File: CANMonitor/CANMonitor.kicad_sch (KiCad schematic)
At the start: 8 parts, among them J1 Screw_Terminal_01x04, J2 Screw_Terminal_01x04, U1 MCP2558FD-xSN

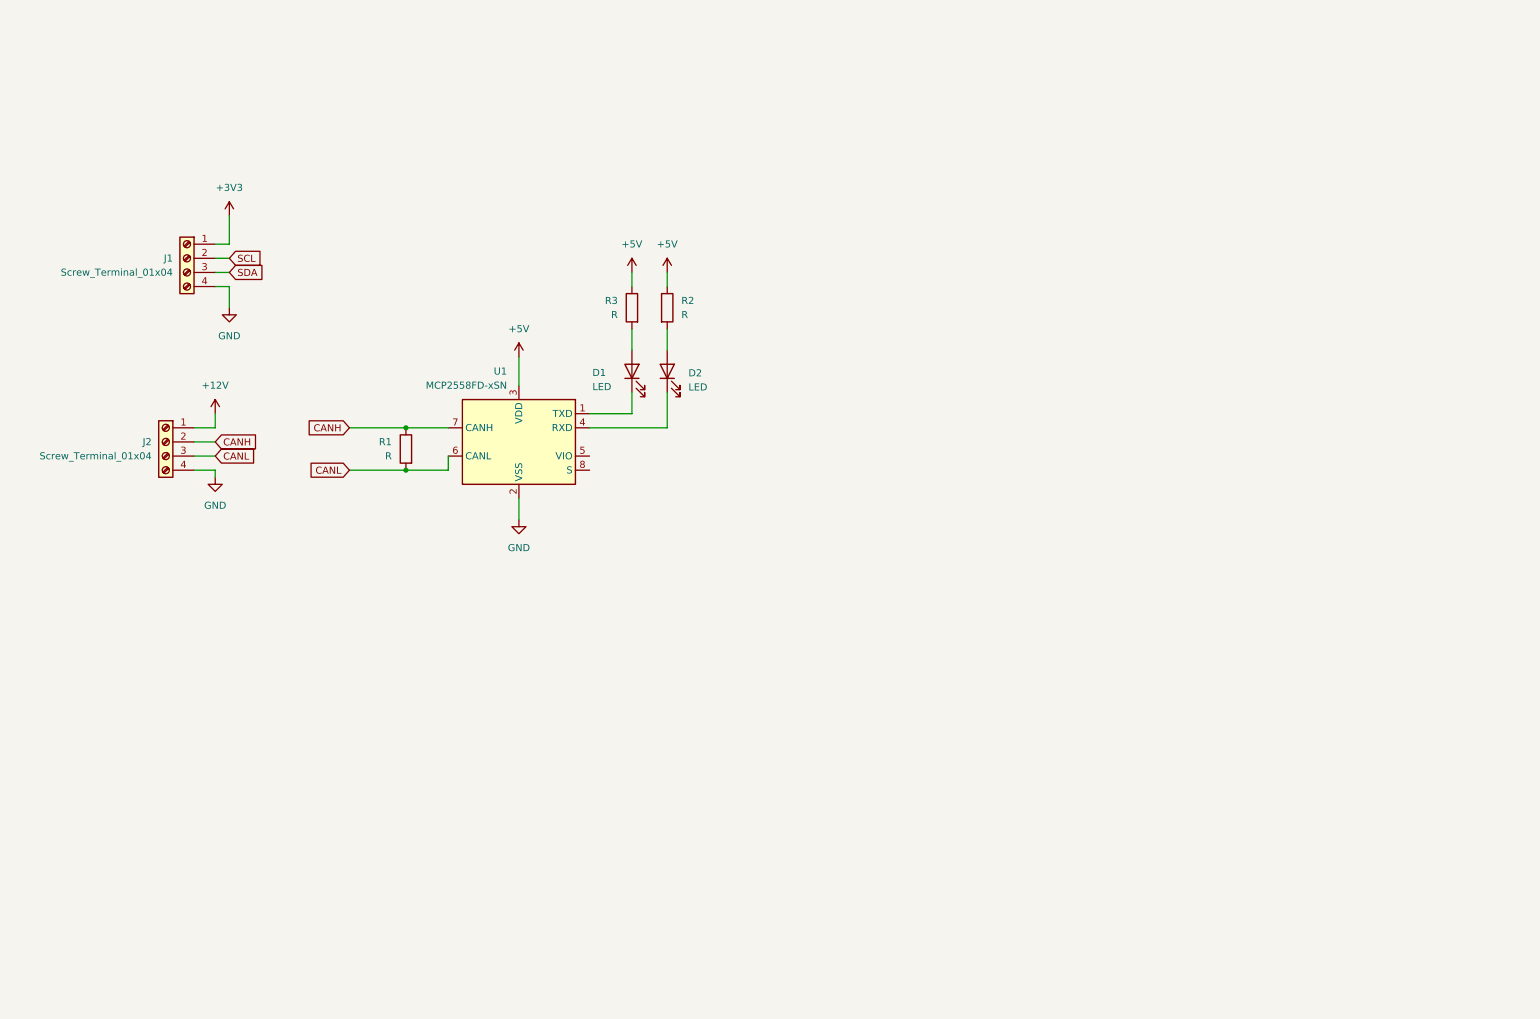
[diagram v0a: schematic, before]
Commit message: Added MCU, netlist, and organized into modules.
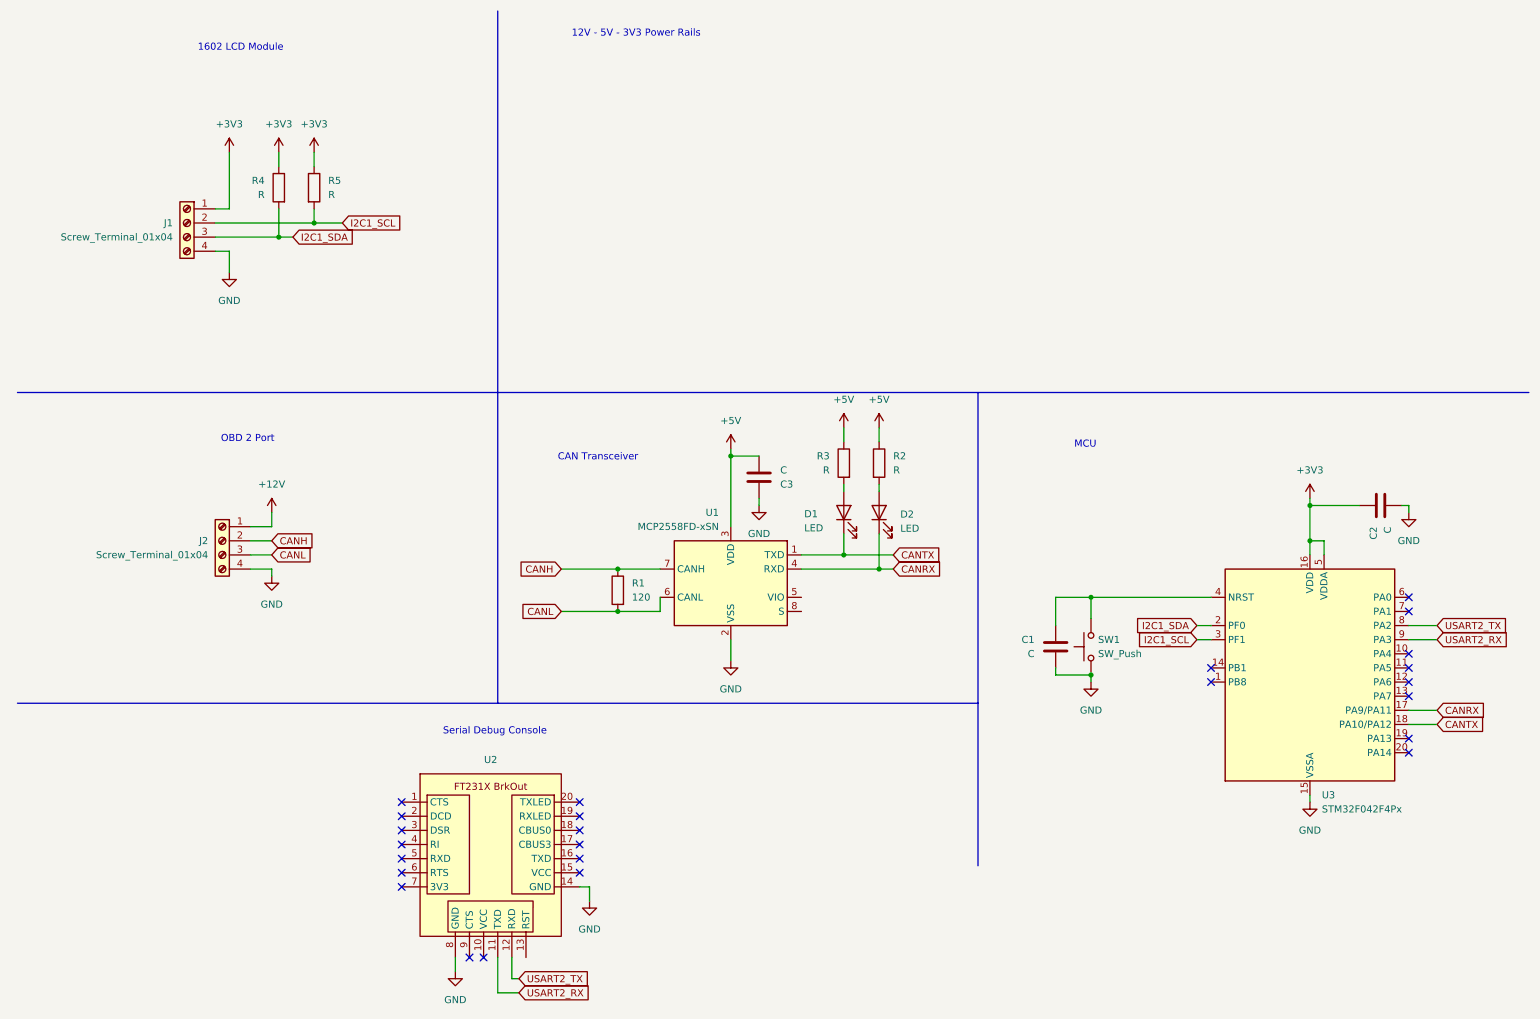
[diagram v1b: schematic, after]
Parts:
- added C1, C2, C3: C, symbol Device:C
- added R4, R5: R, symbol Device:R
- added SW1: SW_Push, symbol Switch:SW_Push
- added U2: (no value), symbol Local_Hats:HEADER_FTDI
- added U3: STM32F042F4Px, Package_SO:TSSOP-20_4.4x6.5mm_P0.65mm, symbol MCU_ST_STM32F0:STM32F042F4Px
- R1: value R -> 120
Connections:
- net +3V3: now also C2.1, R4.1, R5.1, U3.16 (VDD), U3.5 (VDDA)
- net +5V: now also C3.2
- net GND: now also C1.2, C2.2, C3.1, SW1.1, U2.14 (GND), U2.8 (GND), U3.15 (VSSA)
- net CANRX: now reaches D2.1 (K), U1.4 (RXD)
- net CANRX: now also U3.17 (PA9/PA11)
- net CANTX: now reaches D1.1 (K), U1.1 (TXD)
- net CANTX: now also U3.18 (PA10/PA12)
- net SCL renamed I2C1_SCL
- net I2C1_SCL: now also R5.2, U3.3 (PF1)
- net SDA renamed I2C1_SDA
- net I2C1_SDA: now also R4.2, U3.2 (PF0)
- new net: C1.1, SW1.2, U3.4 (NRST)
- new net USART2_RX: U2.11 (TXD), U3.9 (PA3)
- new net USART2_TX: U2.12 (RXD), U3.8 (PA2)
- no-connect marks 0 -> 25
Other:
- note added: "12V - 5V - 3V3 Power Rails"
- note added: "1602 LCD Module"
- note added: "CAN Transceiver"
- note added: "MCU"
- note added: "OBD 2 Port"
- note added: "Serial Debug Console"
- title: (none) -> CANMonitor
- moved on the sheet: D1, D2, J1, J2, R1, R2, R3, U1

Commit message: Created Local Symbols and Added SWD Interface
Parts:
- removed J1, J2: Screw_Terminal_01x04, symbol Connector:Screw_Terminal_01x04
- removed SW1: SW_Push, symbol Switch:SW_Push
- added J3: (no value), symbol Local_Header:Header_Pin_1x4_2.54mm
- added SW1: Switch_PushBtn, symbol Local_Switches:Switch_PushBtn
- added TB1, TB2: (no value), symbol Local_ScrewTerm:Screw_Terminal_01x04
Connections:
- net +12V: now also TB2.1
- net +3V3: now also J3.1, TB1.1
- net CANH: now also TB2.2
- net CANL: now also TB2.3
- net GND: now also J3.5, SW1.2, TB1.4, TB2.4
- net I2C1_SCL: now also TB1.2
- net I2C1_SDA: now also TB1.3
- net NRST: now reaches C1.1, U3.4 (NRST)
- net NRST: now also J3.4, SW1.1
- net SWDIO: now reaches U3.19 (PA13)
- net SWDIO: now also J3.2
- net SWCLK: now reaches U3.20 (PA14)
- net SWCLK: now also J3.3
- no-connect marks 25 -> 24
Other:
- note added: "SWD Header"

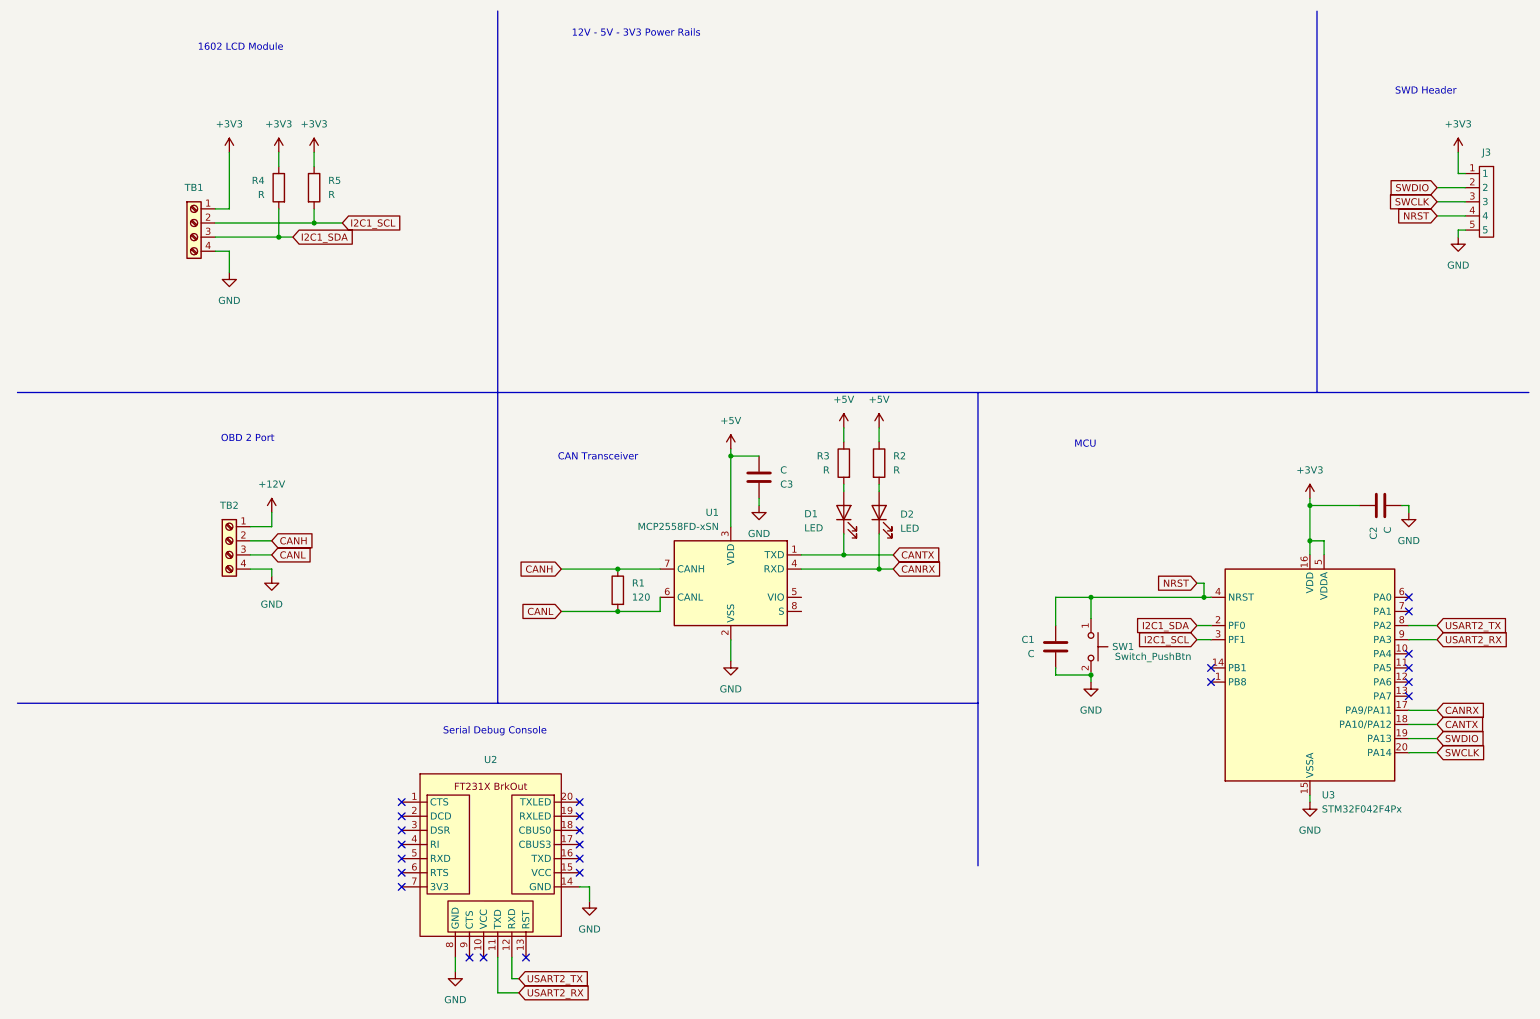
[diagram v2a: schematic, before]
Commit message: Added Custom Symbols and Power LEDs
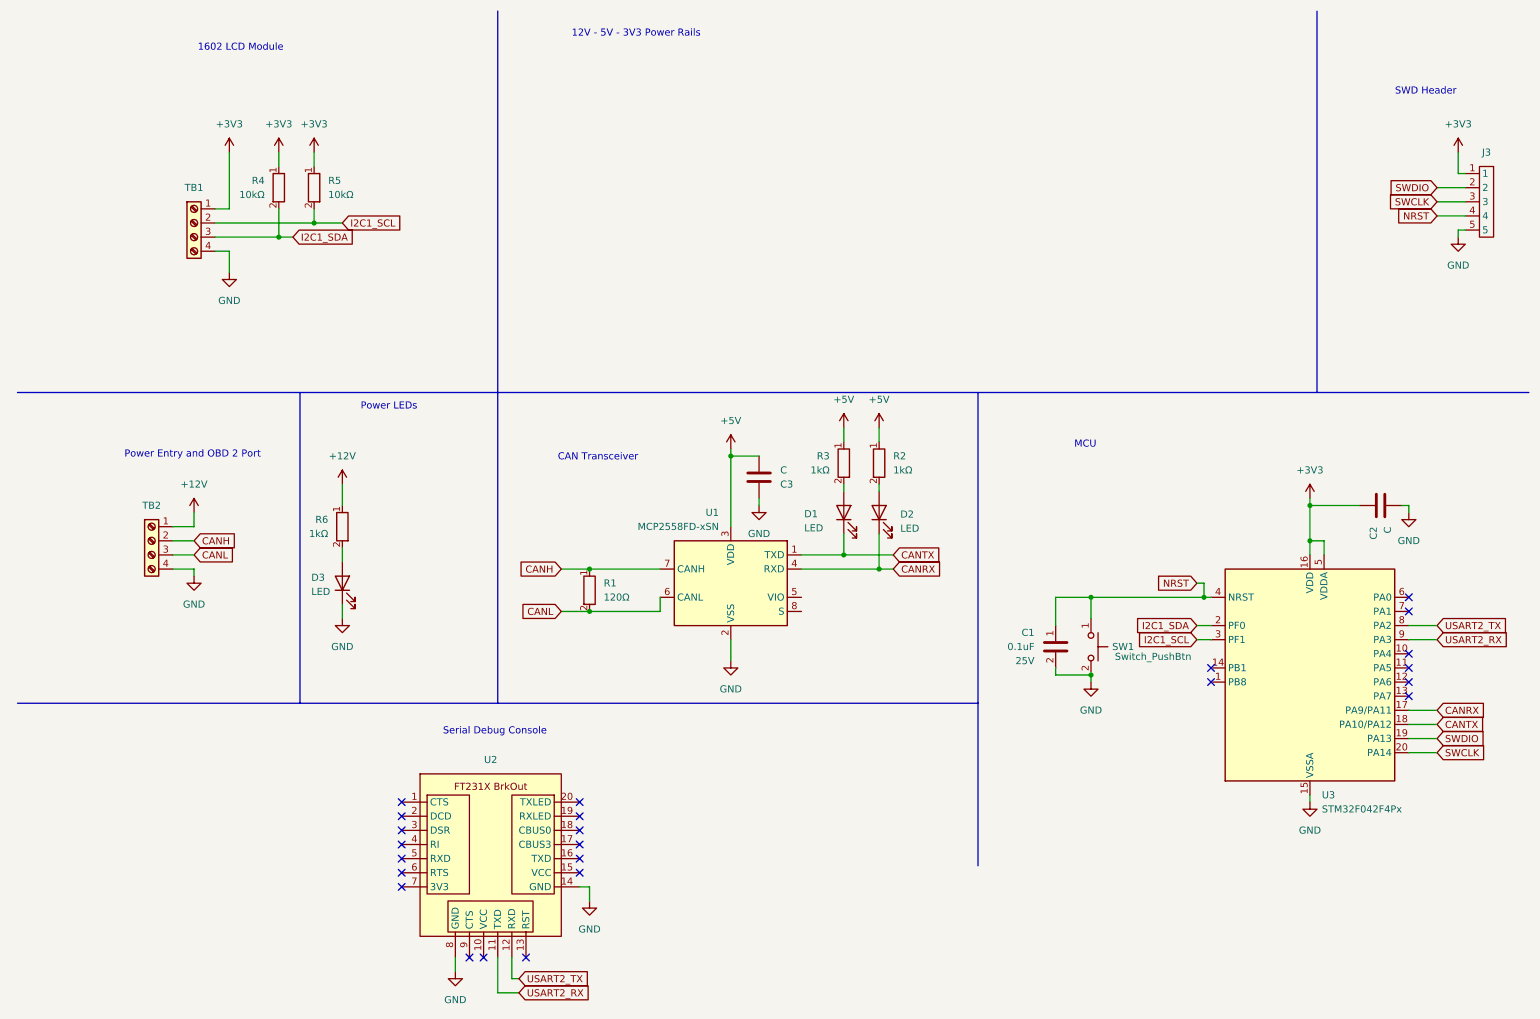
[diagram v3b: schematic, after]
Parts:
- removed C1: C, symbol Device:C
- removed R1: 120, symbol Device:R
- removed R2, R3, R4, R5: R, symbol Device:R
- added C1: 0.1uF, symbol Local_Capacitors_TH:Cap_Cer_0.1uF_25V_TH
- added D3: LED, symbol Device:LED
- added R1: 120Ω, symbol Local_Resistors_TH:Res_120_250mW
- added R2, R3, R6: 1kΩ, symbol Local_Resistors_TH:Res_1k_250mW
- added R4, R5: 10kΩ, symbol Local_Resistors_TH:Res_10k_250mW
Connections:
- net +12V: now also R6.1
- net +3V3: now also R4.1, R5.1
- net +5V: now also R2.1, R3.1
- net CANH: now also R1.1
- net CANL: now also R1.2
- net GND: now also C1.2, D3.1 (K)
- net I2C1_SCL: now also R5.2
- net I2C1_SDA: now also R4.2
- net NRST: now also C1.1
- net at D2.2 (A): now also R2.2
- net at D1.2 (A): now also R3.2
- new net: D3.2 (A), R6.2
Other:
- note added: "Power Entry and OBD 2 Port"
- note added: "Power LEDs"
- note removed: "OBD 2 Port"
- moved on the sheet: TB2
